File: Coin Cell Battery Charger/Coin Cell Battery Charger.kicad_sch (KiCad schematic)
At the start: 2 parts, among them J1 USB_B_Micro

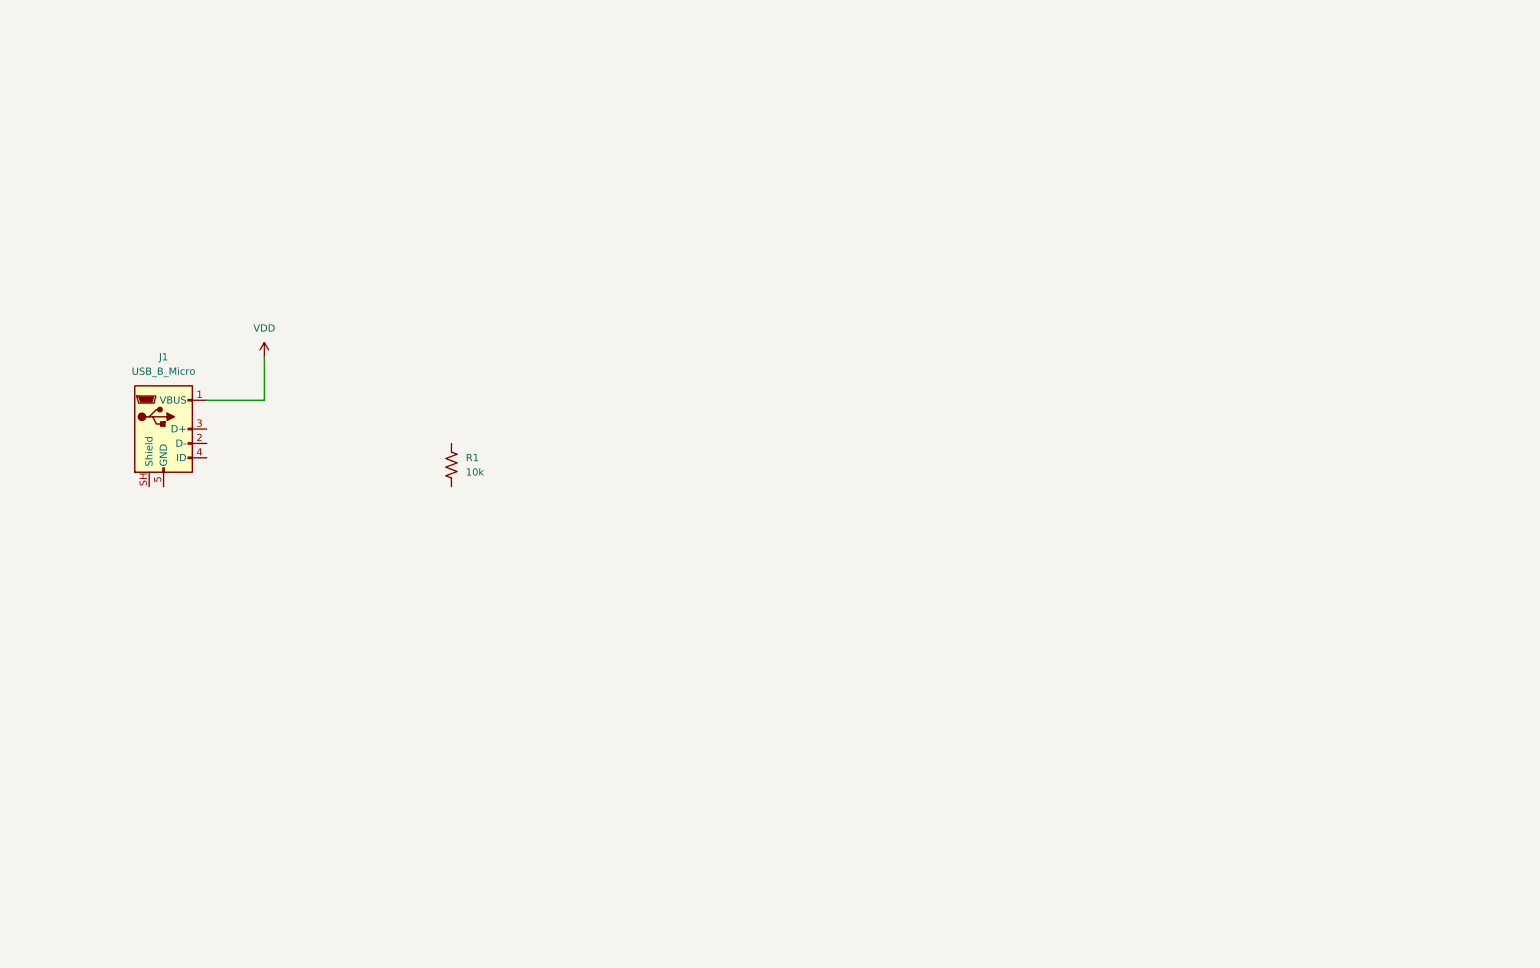
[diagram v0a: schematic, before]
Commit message: Initial Schematic layout
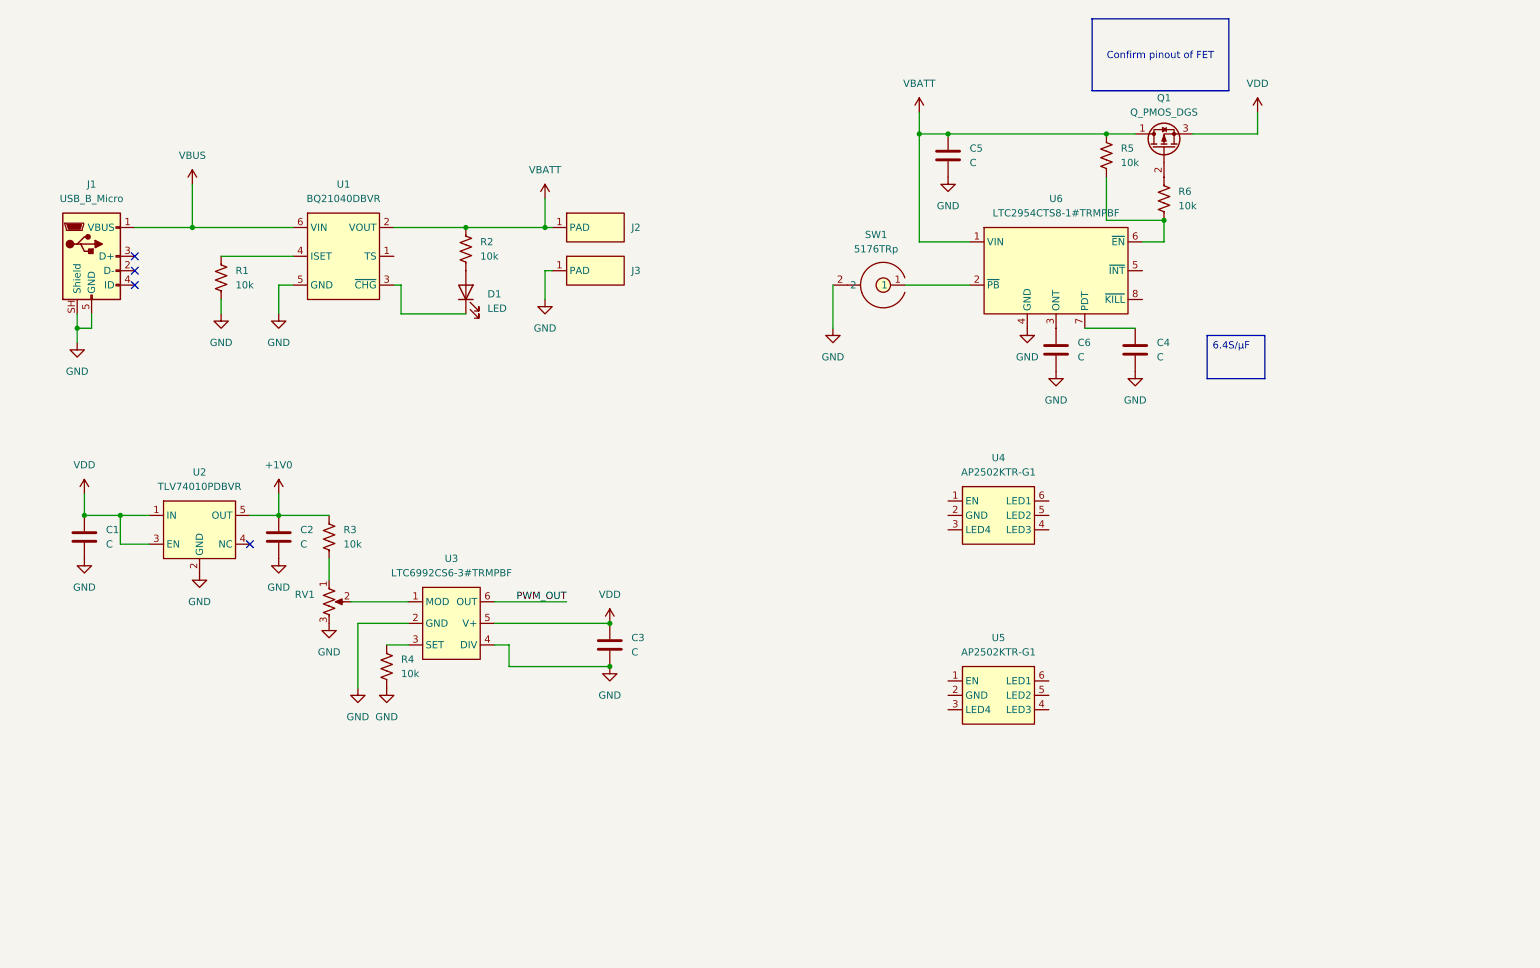
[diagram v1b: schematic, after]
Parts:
- added C1, C2, C3, C4, C5, C6: C, symbol Device:C
- added D1: LED, symbol Device:LED
- added J2, J3: (no value), _Dylan_IC:Solder_Pad_0.6mmx2mm, symbol Dylan Components:Solder_Pad_0.6mmx2mm
- added Q1: Q_PMOS_DGS, symbol Transistor_FET:Q_PMOS_DGS
- added R2, R3, R4, R5, R6: 10k, Resistor_SMD:R_0603_1608Metric_Pad0.98x0.95mm_HandSolder, symbol Device:R_US
- added RV1: R_Potentiometer_US, symbol Device:R_Potentiometer_US
- added SW1: 5176TRp, _Dylan_IC:Keystone_5176TR, symbol Dylan Components:5176TR
- added U1: BQ21040DBVR, Package_TO_SOT_SMD:SOT-23-6, symbol Dylan Components:BQ21040DBVR
- added U2: TLV74010PDBVR, Package_TO_SOT_SMD:SOT-23-5_HandSoldering, symbol Dylan Components:TLV74010PDBVR
- added U3: LTC6992CS6-3#TRMPBF, Package_TO_SOT_SMD:TSOT-23-6, symbol Dylan Components:LTC6992CS6-3#TRMPBF
- added U4, U5: AP2502KTR-G1, Package_TO_SOT_SMD:SOT-23-6, symbol Dylan Components:AP2502KTR-G1
- added U6: LTC2954CTS8-1#TRMPBF, Package_TO_SOT_SMD:TSOT-23-8, symbol Dylan Components:LTC2954CTS8-1#TRMPBF
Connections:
- net VDD: now also C1.1, C3.1, Q1.3 (S), U2.1 (IN), U2.3 (EN), U3.5 (V+); no longer J1.1 (VBUS)
- net GND: now reaches J1.5 (GND)
- net GND: now also J1.SH (Shield), R1.2, C1.2, C2.2, C3.2, C4.2, C5.2, C6.2, J3.1 (PAD), R4.2, RV1.3, SW1.2, U1.5 (GND), U2.2 (GND), U3.2 (GND), U3.4 (DIV), U6.4 (GND)
- net at R1.1: now also U1.4 (ISET)
- new net: C4.1, U6.7 (PDT)
- new net: D1.1 (K), U1.3 (~{CHG})
- new net: D1.2 (A), R2.2
- new net: RV1.2, U3.1 (MOD)
- new net: R4.1, U3.3 (SET)
- new net: Q1.2 (G), R6.1
- new net: SW1.1, U6.2 (~{PB})
- new net: C6.1, U6.3 (ONT)
- new net: R5.2, R6.2, U6.6 (~{EN})
- new net: R3.2, RV1.1
- new net +1V0: C2.1, R3.1, U2.5 (OUT)
- new net PWM_OUT: U3.6 (OUT)
- new net VBATT: C5.1, J2.1 (PAD), Q1.1 (D), R2.1, R5.1, U1.2 (VOUT), U6.1 (VIN)
- new net VBUS: J1.1 (VBUS), U1.6 (VIN)
- no-connect marks 0 -> 4
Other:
- moved on the sheet: J1, R1

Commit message: Touch Ups of Schematic
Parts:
- removed Q1: Q_PMOS_DGS, symbol Transistor_FET:Q_PMOS_DGS
- added D10, D3, D4, D5, D6, D7, D8, D9: ASMD-CWG7-NX7J2, _Dylan_IC:BroadCom_ASMD-CWG7-NX7J2, symbol Dylan Components:ASMD-CWG7-NX7J2
- added Q2: Q_PMOS_GSD, Package_TO_SOT_SMD:SOT-23, symbol Transistor_FET:Q_PMOS_GSD
- added R7, R8: 10k, Resistor_SMD:R_0603_1608Metric_Pad0.98x0.95mm_HandSolder, symbol Device:R_US
- C1, C2: value C -> 10µF
- C3, C5: value C -> 100nF
- C4, C6: value C -> 0.33µF
- R1: value 10k -> 1kΩ
- R2: value 10k -> 1.5kΩ
- R3, R4: value 10k -> 10kΩ
- RV1: footprint (none) -> _Dylan_IC:Bourns_TC33X-2-104E; MFG (none) -> Bourns; MFG PN (none) -> TC33X-2-104E
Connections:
- net GND: now also U4.2 (GND), U5.2 (GND)
- net PWM_OUT: now also U4.1 (EN), U5.1 (EN)
- net VBATT: now also Q2.2 (S)
- net VDD: now also D10.1, D3.1, D4.1, D5.1, D6.1, D7.1, D8.1, D9.1, Q2.3 (D)
- net at U4.3 (LED4): now also D6.2
- net at U4.4 (LED3): now also D5.2
- net at U4.5 (LED2): now also D4.2
- net at U4.6 (LED1): now also D3.2
- net at R6.1: now also Q2.1 (G)
- net at U5.3 (LED4): now also D10.2
- net at U5.4 (LED3): now also D9.2
- net at U5.5 (LED2): now also D8.2
- net at U5.6 (LED1): now also D7.2
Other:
- moved on the sheet: U4, U5

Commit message: Initial Layout done
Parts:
- removed J1: USB_B_Micro, symbol Connector:USB_B_Micro
- added C7: 10µF, Capacitor_SMD:C_0603_1608Metric, symbol Device:C
- added C8, C9: 100nF, Capacitor_SMD:C_0603_1608Metric, symbol Device:C
- added D2: D_TVS, Diode_SMD:D_SOD-923, symbol Device:D_TVS
- added J1: 0473461001, _Dylan_IC:Molex_0473461001, symbol Dylan Components:0473461001
- added R9: 10kΩ, Resistor_SMD:R_0603_1608Metric_Pad0.98x0.95mm_HandSolder, symbol Device:R_US
- C1, C2, C3, C4, C5, C6: footprint (none) -> Capacitor_SMD:C_0603_1608Metric
- D1: footprint (none) -> LED_SMD:LED_0603_1608Metric; MFG (none) -> Lite-ON; MFG PN (none) -> LTST-C190GKT
- Q2: MFG Infineon Technologies -> Diodes Inc; MFG PN BSS84PH6327XTSA2 -> DMP2045U-7
- R1: value 1kΩ -> 3.6kΩ
- R5, R6: value 10k -> 10kΩ
- R7: value 10k -> 100kΩ
- R8: value 10k -> 28.7kΩ
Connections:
- net GND: now also R8.2, C7.2, C8.2, C9.2, D2.1 (A1), J1.5 (GND), J1.SH (Shield), R9.2
- net VBATT: now also C8.1
- net VBUS: now also C7.1, D2.2 (A2), J1.1 (VBUS)
- net VDD: now also R7.1, C9.1
- net at U1.1 (TS): now also R9.1
- net at U6.8 (~{KILL}): now also R7.2, R8.1
- no-connect marks 4 -> 5
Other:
- title: (none) -> LIT CHIP GEN 2.0
- moved on the sheet: D1, J2, J3, R1, R2, R8, U1

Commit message: Resized PCB to be 30mm OD, added vertical connector option, Electrical layout incomplete
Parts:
- removed SW1: 5176TRp, _Dylan_IC:Keystone_5176TR, symbol Dylan Components:5176TR
- added H1, H2: MountingHole, MountingHole:MountingHole_3.2mm_M3, symbol Mechanical:MountingHole
- added J4: UJ2-MIBV-4-SMT-TR-67, _Dylan_IC:SameSky_UJ2-MIBV-4-SMT-TR-67, symbol Dylan Components:UJ2-MIBV-4-SMT-TR-67
- added SW1: 5136TR, _Dylan_IC:Keystone_5136TR, symbol Dylan Components:5136TR
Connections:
- net GND: now also J4.5 (GND), J4.SH (Shield), SW1.2
- net VBUS: now also J4.1 (VBUS)
- net at U6.2 (~{PB}): now also SW1.1
- no-connect marks 5 -> 8

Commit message: TP Added + M2 mounting holes
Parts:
- added R10, R11: 1Ω, Resistor_SMD:R_0603_1608Metric_Pad0.98x0.95mm_HandSolder, symbol Device:R_US
- added TP1, TP2, TP3, TP4, TP5, TP6, TP7: TestPoint, TestPoint:TestPoint_Pad_D1.0mm, symbol Connector:TestPoint
- H1, H2: footprint MountingHole:MountingHole_3.2mm_M3 -> MountingHole:MountingHole_2.2mm_M2_ISO14580
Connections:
- net +1V0: now also TP5.1
- net GND: now also TP7.1
- net PWM_OUT: now also TP6.1
- net VBATT: now also TP2.1
- net VBUS: now also TP1.1
- net VDD: now also TP3.1
- net at U4.3 (LED4): now also R10.1; no longer D6.2
- net at U5.3 (LED4): now also R11.1; no longer D10.2
- net at SW1.1, U6.2 (~{PB}): now also TP4.1
- new net: D10.2, R11.2
- new net: D6.2, R10.2

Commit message: Added silk screen final touches, all PCBs 0.8mm, updated Fmod,
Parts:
- R4: value 10kΩ -> 500kΩ
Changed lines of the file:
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@@
 			)
 		)
-		(property "Value" "10kΩ"
+		(property "Value" "500kΩ"
 			(at 82.55 132.0799 0)
 			(show_name no)
